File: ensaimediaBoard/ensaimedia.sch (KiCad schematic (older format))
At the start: 31 parts, among them J1 USB_B_Micro, J10 -, J11 -, J12 -, J2 POWER, J3 POW_SW, J4 BOOT, J5 UART, J6 ESP_SW, J7 External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

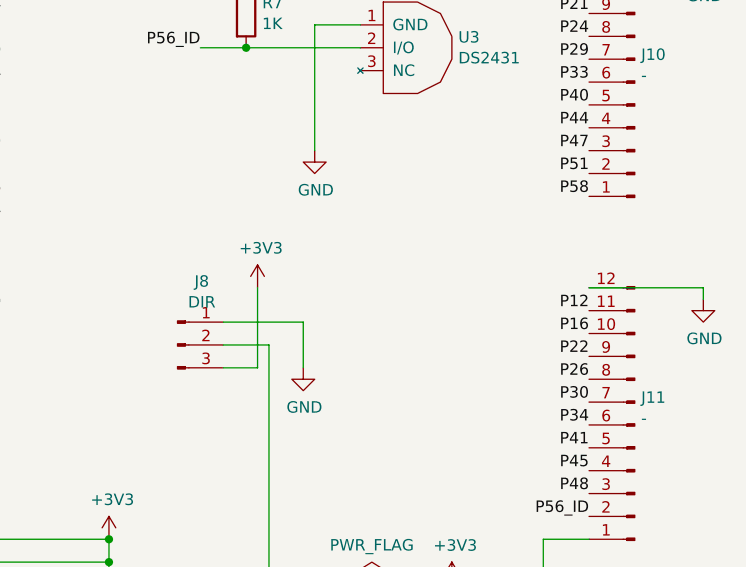
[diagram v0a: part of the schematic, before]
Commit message: Add DIR solder jumper comment in the schematic.
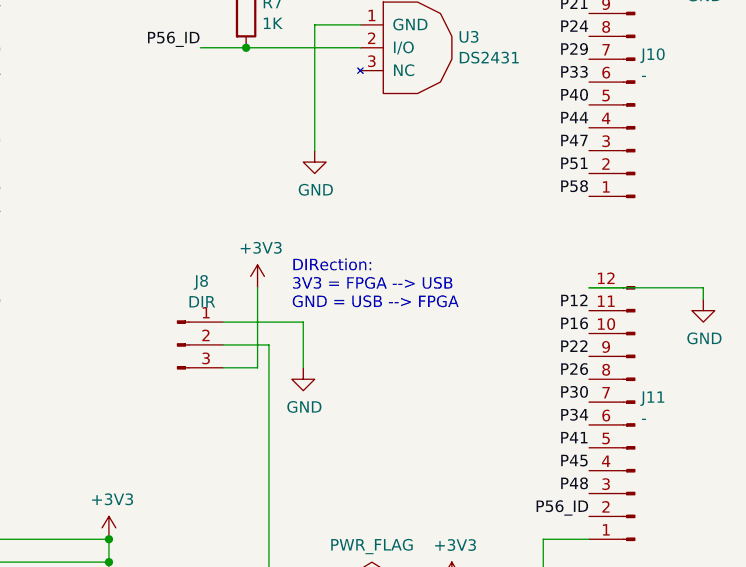
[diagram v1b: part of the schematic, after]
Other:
- note added: "DIRection:\n3V3 = FPGA --> USB\nGND = USB --> FPGA"
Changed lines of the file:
@@
 	5000 1100 4650 1100
 Connection ~ 5000 1100
+Text Notes 8700 3450 0    50   ~ 0
+DIRection:\n3V3 = FPGA --> USB\nGND = USB --> FPGA
 $EndSCHEMATC
